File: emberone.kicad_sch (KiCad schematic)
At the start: 0 parts

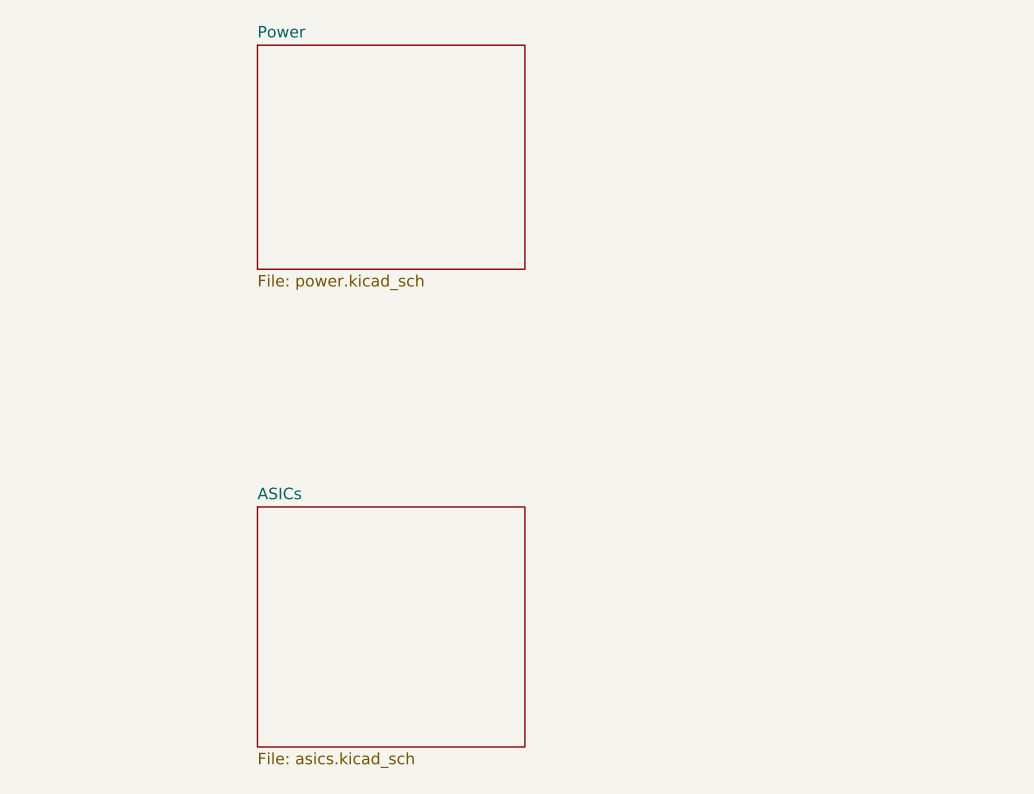
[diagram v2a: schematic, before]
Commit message: schematic done, started initial placement
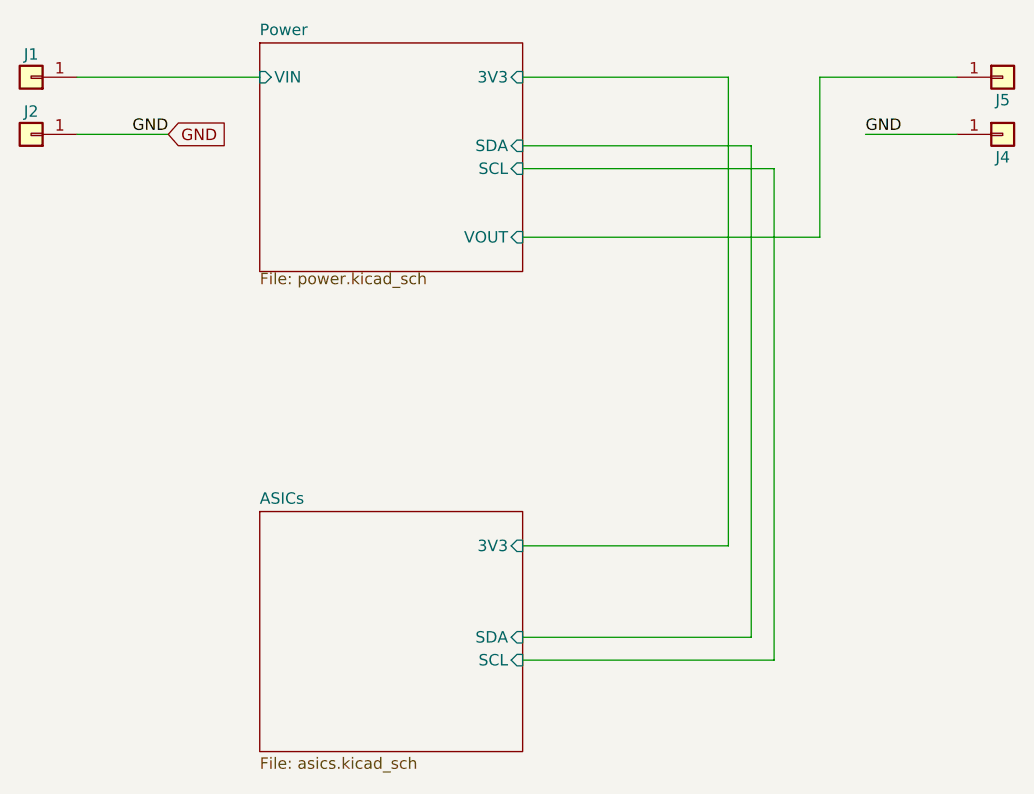
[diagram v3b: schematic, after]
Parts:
- added J1, J2, J4, J5: Screw Terminal, emberone:7770-screw-terminal, symbol Connector_Generic:Conn_01x01
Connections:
- new net GND: J2.1 (Pin_1), J4.1 (Pin_1)
- new net Power/VIN: J1.1 (Pin_1)
- new net Power/VOUT: J5.1 (Pin_1)
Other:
- sheet ASICs ports: added 3V3, SCL, SDA; removed none
- sheet Power ports: added 3V3, SCL, SDA, VIN, VOUT; removed none

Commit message: add iBOM
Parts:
- J1, J2, J4, J5: DK 36-7771-ND -> 36-7770-ND; PARTNO 36-7771 -> 36-7770
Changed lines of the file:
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@@
 			)
 		)
-		(property "DK" "36-7771-ND"
+		(property "DK" "36-7770-ND"
 			(at 152.4 49.53 0)
 			(effects
@@
 			)
 		)
-		(property "PARTNO" "36-7771"
+		(property "PARTNO" "36-7770"
 			(at 152.4 49.53 0)
 			(effects
@@
 			)
 		)
-		(property "DK" "36-7771-ND"
-			(at 44.45 43.18 0)
-			(effects
-				(font
-					(size 1.27 1.27)
-				)
-				(hide yes)
-			)
-		)
-		(property "PARTNO" "36-7771"
+		(property "DK" "36-7770-ND"
+			(at 44.45 43.18 0)
+			(effects
+				(font
+					(size 1.27 1.27)
+				)
+				(hide yes)
+			)
+		)
+		(property "PARTNO" "36-7770"
 			(at 44.45 43.18 0)
 			(effects
@@
 			)
 		)
-		(property "DK" "36-7771-ND"
-			(at 44.45 49.53 0)
-			(effects
-				(font
-					(size 1.27 1.27)
-				)
-				(hide yes)
-			)
-		)
-		(property "PARTNO" "36-7771"
+		(property "DK" "36-7770-ND"
+			(at 44.45 49.53 0)
+			(effects
+				(font
+					(size 1.27 1.27)
+				)
+				(hide yes)
+			)
+		)
+		(property "PARTNO" "36-7770"
 			(at 44.45 49.53 0)
 			(effects
@@
 			)
 		)
-		(property "DK" "36-7771-ND"
-			(at 152.4 43.18 0)
-			(effects
-				(font
-					(size 1.27 1.27)
-				)
-				(hide yes)
-			)
-		)
-		(property "PARTNO" "36-7771"
-			(at 152.4 43.18 0)
-			(effects
+		(property "DK" "36-7770-ND"
+			(at 152.4 43.18 0)
+			(effects
+				(font
+					(size 1.27 1.27)
+				)
+				(hide yes)
+			)
+		)
+		(property "PARTNO" "36-7770"
+			(at 152.4 43.18 0)
+			(effects

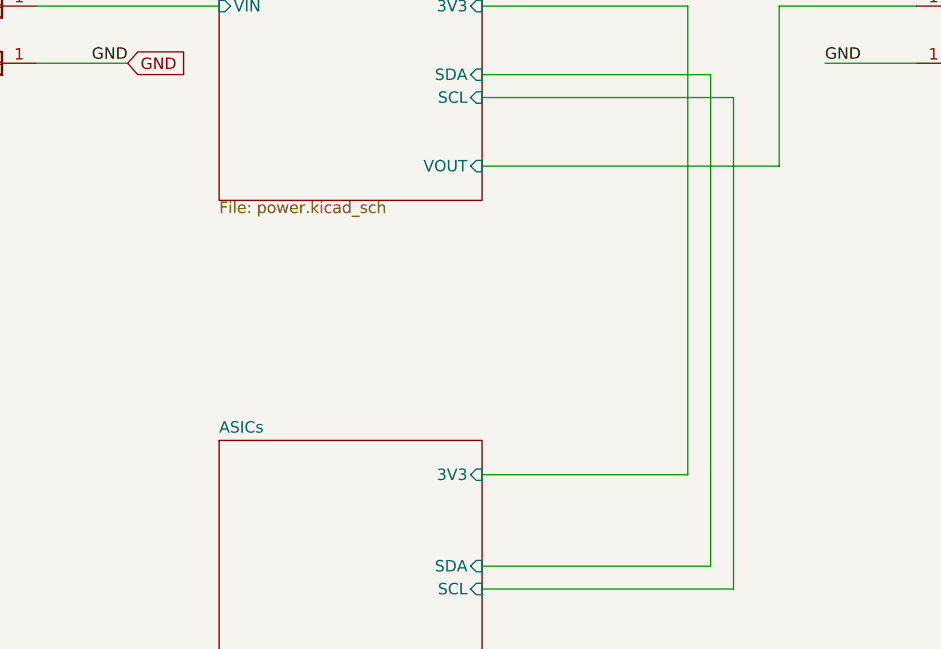
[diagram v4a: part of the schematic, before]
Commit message: adding initial ASIC stacks
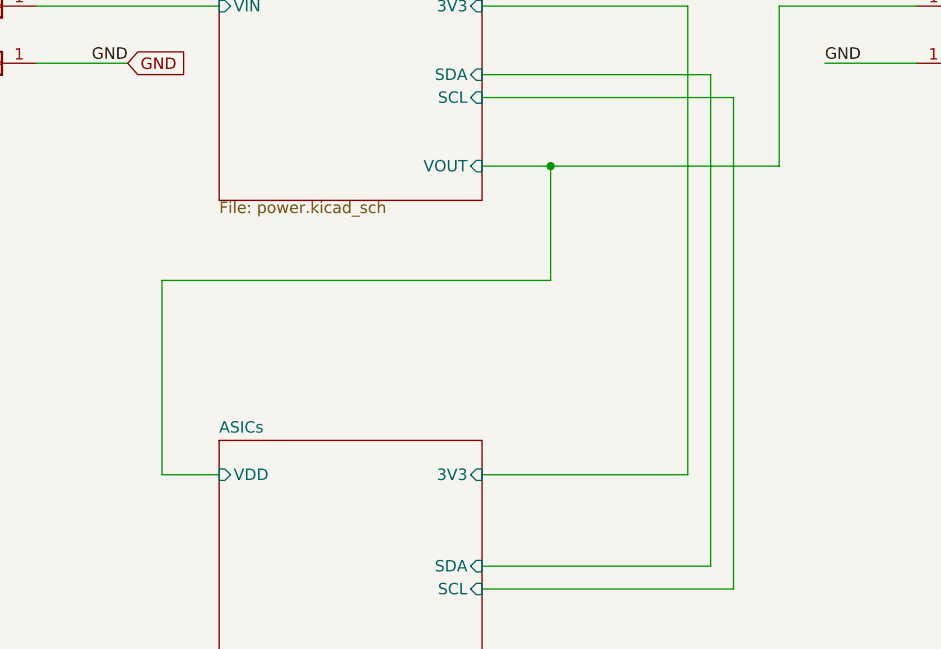
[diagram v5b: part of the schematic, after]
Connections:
- net Power/VOUT renamed ASICs/VDD
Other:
- sheet ASICs ports: added VDD; removed none
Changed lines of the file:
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@@
 		(rev "1")
 	)
+	(junction
+		(at 106.68 60.96)
+		(diameter 0)
+		(color 0 0 0 0)
+	)
 	(wire
 		(pts
@@
 	(wire
 		(pts
+			(xy 106.68 73.66) (xy 106.68 60.96)
+		)
+		(stroke
+			(width 0)
+			(type default)
+		)
+	)
+	(wire
+		(pts
 			(xy 124.46 50.8) (xy 99.06 50.8)
 		)
@@
 	(wire
 		(pts
+			(xy 63.5 95.25) (xy 63.5 73.66)
+		)
+		(stroke
+			(width 0)
+			(type default)
+		)
+	)
+	(wire
+		(pts
 			(xy 121.92 43.18) (xy 99.06 43.18)
 		)
@@
 	(wire
 		(pts
+			(xy 63.5 73.66) (xy 106.68 73.66)
+		)
+		(stroke
+			(width 0)
+			(type default)
+		)
+	)
+	(wire
+		(pts
 			(xy 147.32 49.53) (xy 137.16 49.53)
 		)
@@
 	(wire
 		(pts
+			(xy 69.85 95.25) (xy 63.5 95.25)
+		)
+		(stroke
+			(width 0)
+			(type default)
+		)
+	)
+	(wire
+		(pts
 			(xy 127 53.34) (xy 99.06 53.34)
 		)
@@
 	(wire
 		(pts
-			(xy 132.08 60.96) (xy 99.06 60.96)
+			(xy 106.68 60.96) (xy 99.06 60.96)
+		)
+		(stroke
+			(width 0)
+			(type default)
+		)
+	)
+	(wire
+		(pts
+			(xy 132.08 60.96) (xy 106.68 60.96)
 		)
 		(stroke
@@
 			)
 		)
+		(pin "VDD" input
+			(at 69.85 95.25 180)
+			(effects
+				(font
+					(size 1.27 1.27)
+				)
+				(justify left)
+			)
+		)

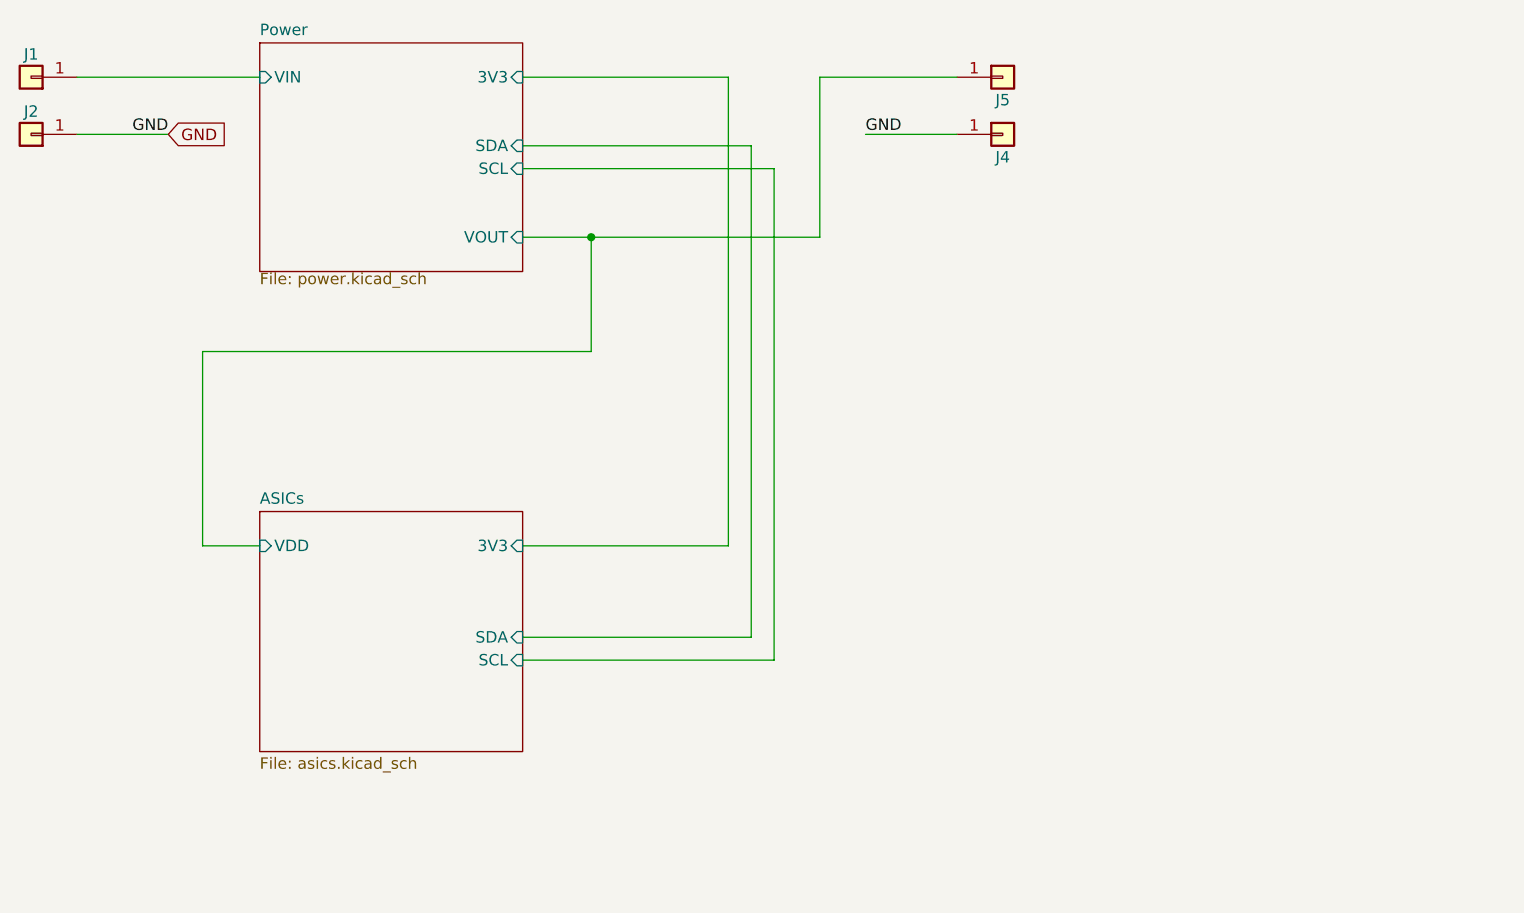
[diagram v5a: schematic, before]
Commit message: added all the ASICs to the schematic. added the RP2040 circuit for data. added the VDDIO boost circuit. schematic cleanup
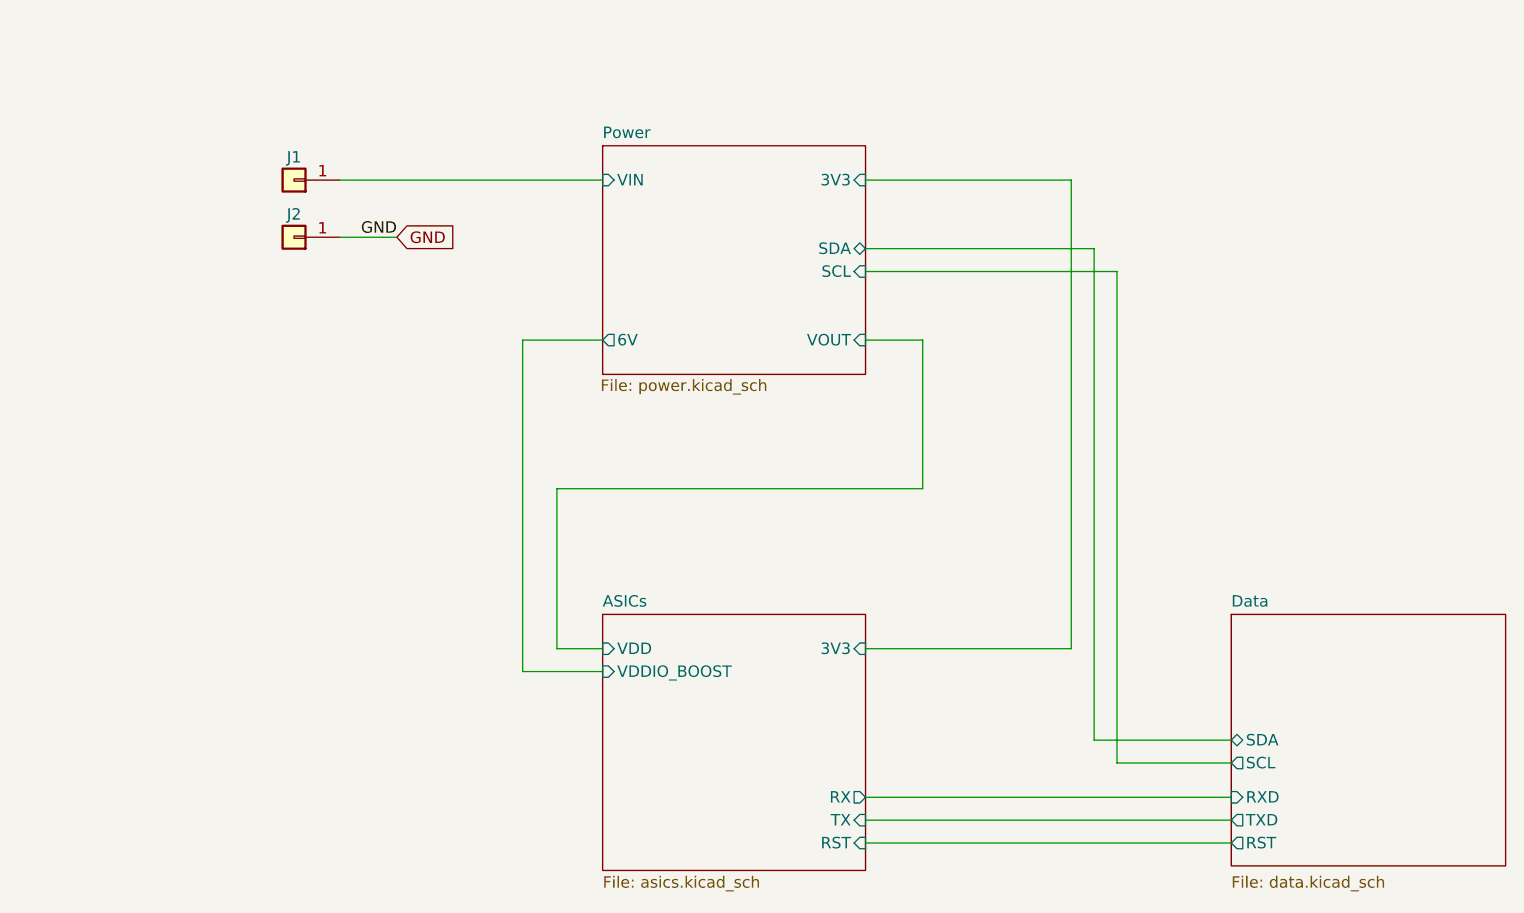
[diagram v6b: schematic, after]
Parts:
- removed J4, J5: Screw Terminal, emberone:7770-screw-terminal, symbol Connector_Generic:Conn_01x01
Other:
- added sheet Data (data.kicad_sch)
- sheet ASICs ports: added RST, RX, TX, VDDIO_BOOST; removed SCL, SDA
- sheet Power ports: added 6V; removed none
- moved on the sheet: J1, J2

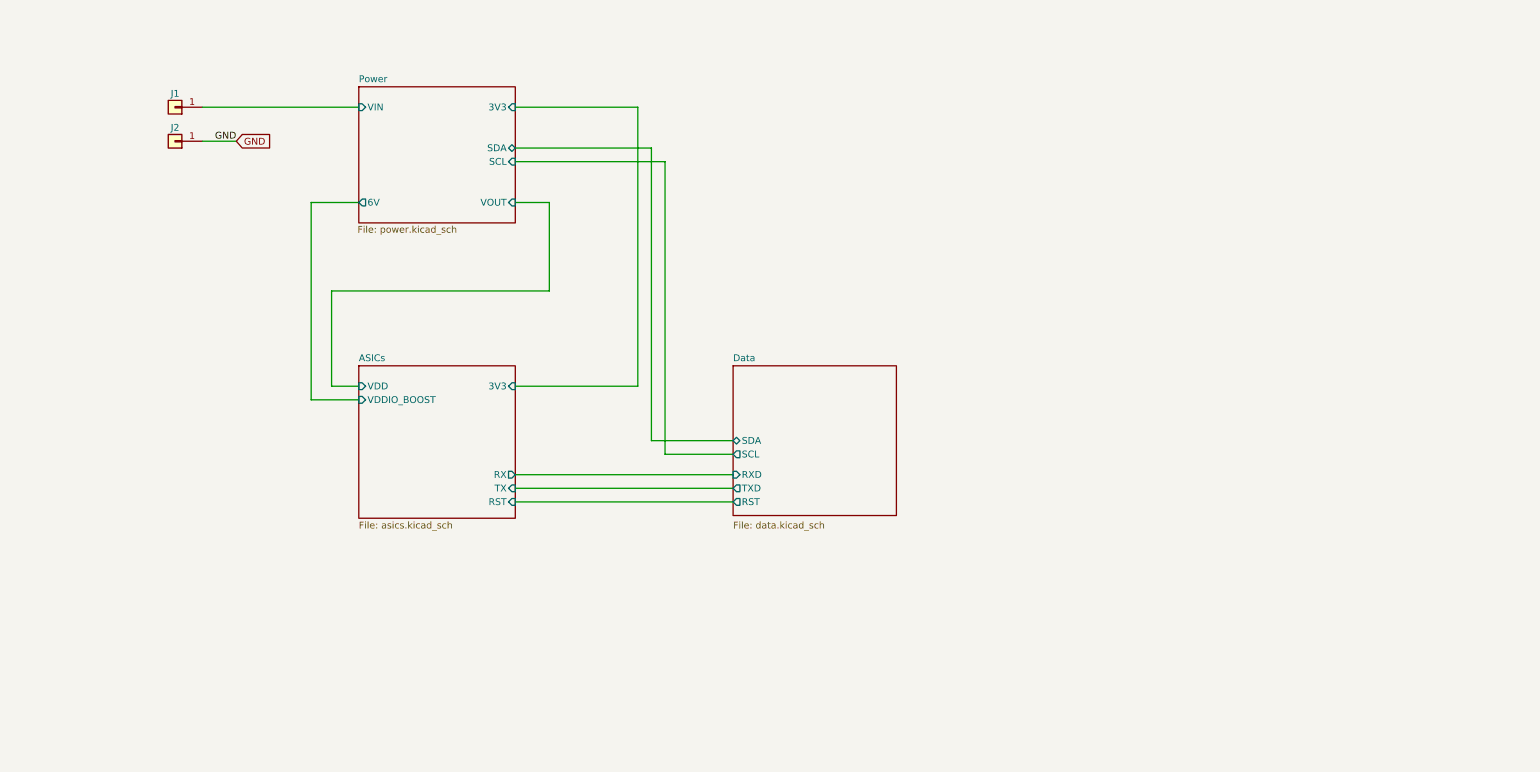
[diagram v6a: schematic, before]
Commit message: added sweet logo to schematic worksheet. Schematic cleanup.
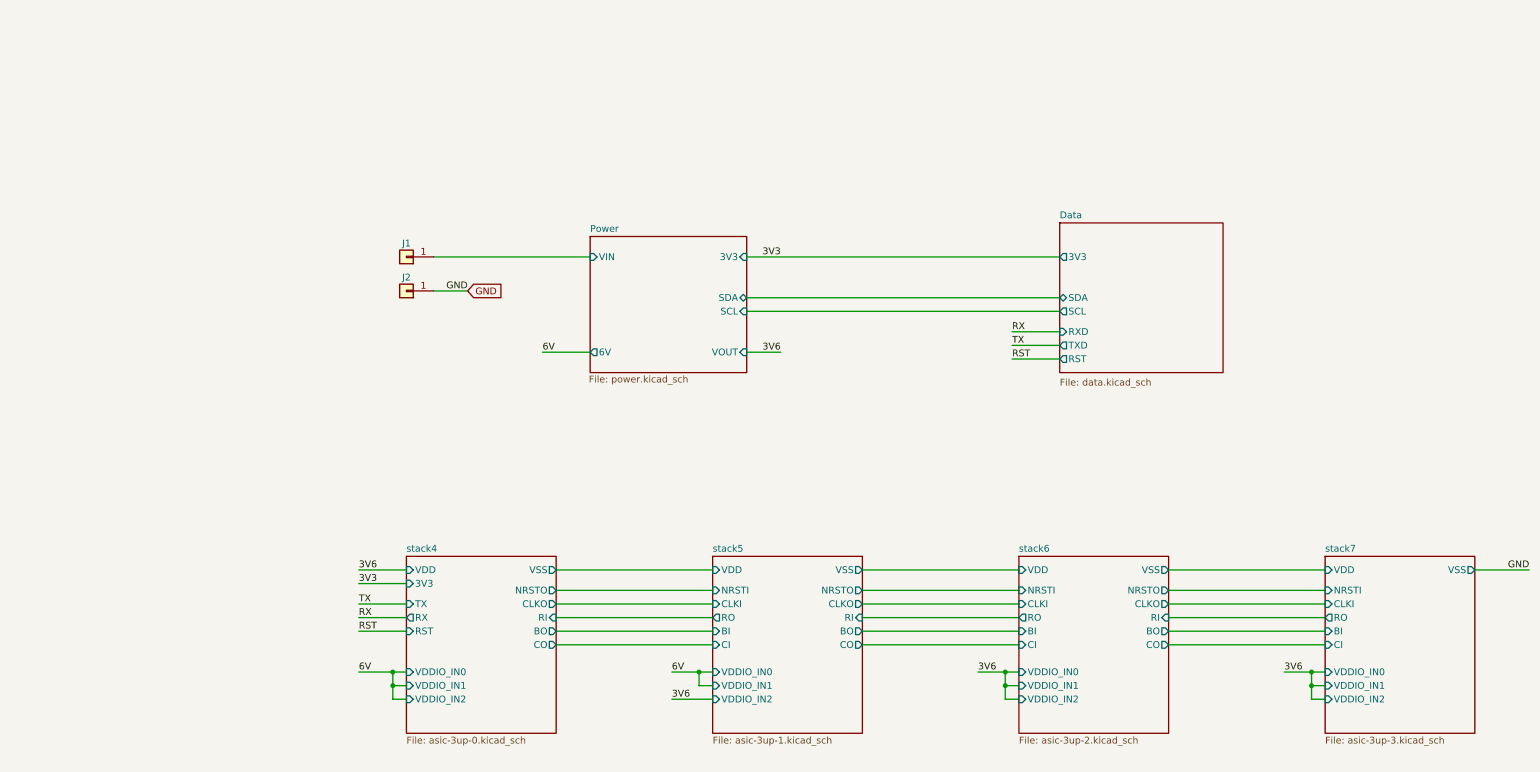
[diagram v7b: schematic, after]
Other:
- removed sheet ASICs
- added sheet stack4 (asic-3up-0.kicad_sch)
- added sheet stack5 (asic-3up-1.kicad_sch)
- added sheet stack6 (asic-3up-2.kicad_sch)
- added sheet stack7 (asic-3up-3.kicad_sch)
- sheet Data ports: added 3V3; removed none
- moved on the sheet: J1, J2
